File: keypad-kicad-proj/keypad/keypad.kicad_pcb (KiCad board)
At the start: 2 copper layers, 3.5 x 3.1 mm, 115 parts, among them J1 Screw_Terminal_01x02, J2 USB4105-GF-A, J3 USB4105-GF-A, J4 Micro_SD_Card_Det_Hirose_DM3AT, Q1 BC817, Q2 BC817, Q3 IRF9393TRPBF, SW1 RotaryEncoder, SW2 RotaryEncoder, SW25 SW_SPST, SW26 Cherry_MX, SW27 Cherry_MX, SW28 Cherry_MX, SW29 SW_SPST, SW30 SW_SPST, SW31 SW_SPST, SW32 Cherry_MX, SW33 Cherry_MX, SW34 Cherry_MX, SW35 SW_SPST, SW36 SW_SPST, SW37 SW_SPST, SW38 Cherry_MX, SW39 Cherry_MX, SW40 Cherry_MX, SW41 SW_SPST, SW42 SW_SPST, SW43 SW_SPST, SW44 Cherry_MX, SW45 Cherry_MX, SW46 Cherry_MX, SW47 SW_SPST, SW48 SW_SPST, SW49 SW_SPST, U1 ESP32-S3-WROOM-1, U10 SK6812MINI-E, U11 SK6812MINI-E, U12 SK6812MINI-E, U13 SK6812MINI-E, U14 SK6812MINI-E, U2 TLV75901PDRVT, U27 SK6812MINI-E, U3 CP2102N-A01-GQFN24, U4 SK6812MINI-E, U5 SK6812MINI-E, U6 SK6812MINI-E, U7 SK6812MINI-E, U8 SK6812MINI-E, U9 SK6812MINI-E

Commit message: inital pcb layout
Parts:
- SW25: value SW_SPST -> SW_RST; footprint Button_Switch_THT:SW_PUSH-12mm_Wuerth-430476085716 -> Button_Switch_THT:SW_PUSH_6mm
- moved S1 239.4 mm to (263.9, 81.8), turned to 90 degrees
- moved SW26 168.1 mm to (187.3, 74.2)
- moved SW44 168.1 mm to (238.7, 74.2)
- moved SW32 168.1 mm to (204.4, 74.2)
- moved SW33 168.1 mm to (204.4, 91.3)
- moved SW34 168.1 mm to (204.4, 108.5)
- moved SW38 168.1 mm to (221.6, 74.2)
- moved SW39 168.1 mm to (221.6, 91.3)
- moved SW40 168.1 mm to (221.6, 108.5)
- moved SW27 168.1 mm to (187.3, 91.3)
- moved SW28 168.1 mm to (187.3, 108.5)
- moved SW45 168.1 mm to (238.7, 91.3)
- moved SW46 168.1 mm to (238.7, 108.5)
- moved SW1 148.6 mm to (254.5, 48.5), turned to -90 degrees
- moved J3 143.1 mm to (217.2, 30.7), turned to 180 degrees
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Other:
- board size 3.5 x 3.1 mm -> 100 x 100 mm

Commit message: pcb layout update
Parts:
- Brd1: footprint Connector_PinHeader_1.00mm:PinHeader_1x04_P1.00mm_Vertical -> PUT_RocketLab_other:128x64OLED_V2
- C1, C10, C11, C12, C13, C14, C2, C3, C4, C5, C6, C7, C8, C9, D14, D15, D16, D17, D18, D20, D22, D23, D24, D25, D28, D29, D30, D31, D32, D33, D34, D35, D36, D37, D38, D39, J1, J4, Q1, Q2, Q3, R1, R10, R11, R12, R13, R14, R15, R16, R17, R18, R19, R2, R20, R21, R3, R4, R5, R6, R7, R8, R9, U1, U10, U11, U12, U13, U14, U2, U27, U3, U4, U5, U6, U7, U8, U9: moved to B.Cu
- moved J3 242.0 mm to (-24.4, 42.9)
- moved J2 204.9 mm to (-17.7, 161.2), turned to 180 degrees
- moved D18 172.2 mm to (-21.7, 54.0), turned to 90 degrees
- moved R5 166.1 mm to (-23.3, 59.0), turned to -90 degrees
- moved R7 162.8 mm to (-23.0, 62.1), turned to -90 degrees
- moved C5 159.8 mm to (-20.8, 62.1), turned to -90 degrees
- moved Q3 157.9 mm to (156.4, 50.0)
- moved U2 156.1 mm to (166.1, 57.5)
- moved D16 154.4 mm to (-20.8, 171.0), turned to -90 degrees
- moved R10 153.4 mm to (-1.00, 45.6), turned to 90 degrees
- moved D15 153.1 mm to (-18.5, 171.0), turned to -90 degrees
- moved SW30 151.8 mm to (-45.0, 225.5)
- moved SW36 151.8 mm to (-28.0, 225.5)
- moved SW42 151.8 mm to (-10.9, 225.5)
- moved SW48 151.8 mm to (6.15, 225.5)
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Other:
- board size 100 x 100 mm -> 169.5 x 132.2 mm

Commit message: full inital pcb layout
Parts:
- D19, D21: moved to B.Cu
- moved J2 190.2 mm to (130.9, 42.5)
- moved D15 190.2 mm to (130.1, 52.3)
- moved D16 190.2 mm to (127.7, 52.3)
- moved D17 190.2 mm to (133.9, 53.9)
- moved Q1 111.9 mm to (98.9, 88.7)
- moved R10 111.9 mm to (102.1, 89.1)
- moved R7 109.9 mm to (83.4, 89.6), turned to 0 degrees
- moved R5 108.1 mm to (80.3, 89.9), turned to 0 degrees
- moved C5 107.3 mm to (83.4, 87.4), turned to 0 degrees
- moved D18 102.8 mm to (75.3, 88.2), turned to 180 degrees
- moved D21 100.9 mm to (83.2, 81.2)
- moved D19 99.8 mm to (83.2, 78.6)
- moved J3 97.9 mm to (63.9, 85.2), turned to -90 degrees
- moved Q2 97.5 mm to (91.6, 88.4)
- moved R11 97.5 mm to (95.0, 88.9)
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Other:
- board size 169.5 x 132.2 mm -> 132.9 x 112.7 mm

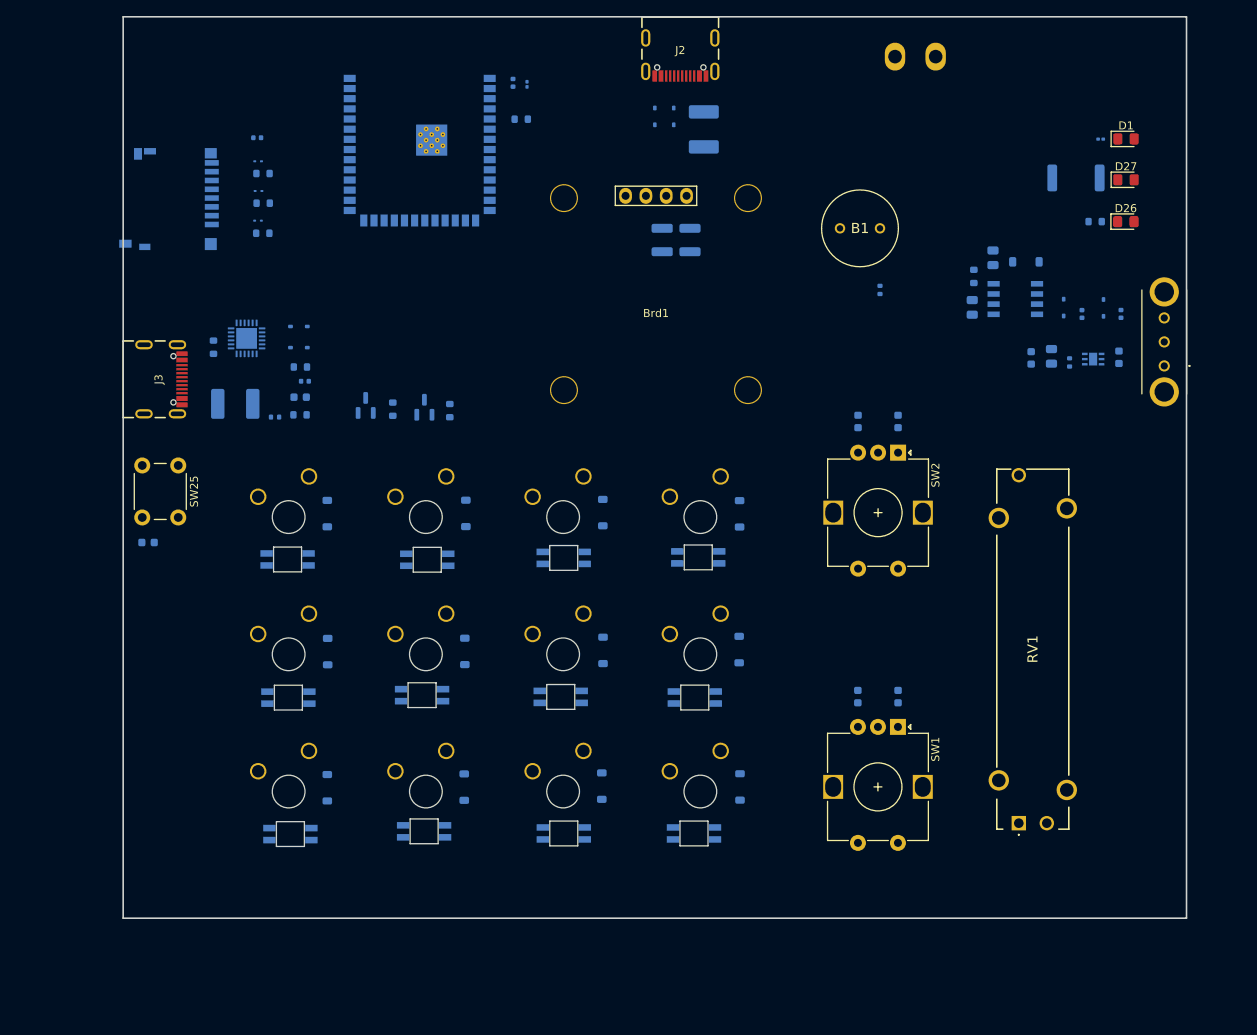
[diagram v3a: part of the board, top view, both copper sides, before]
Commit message: update keys alignment
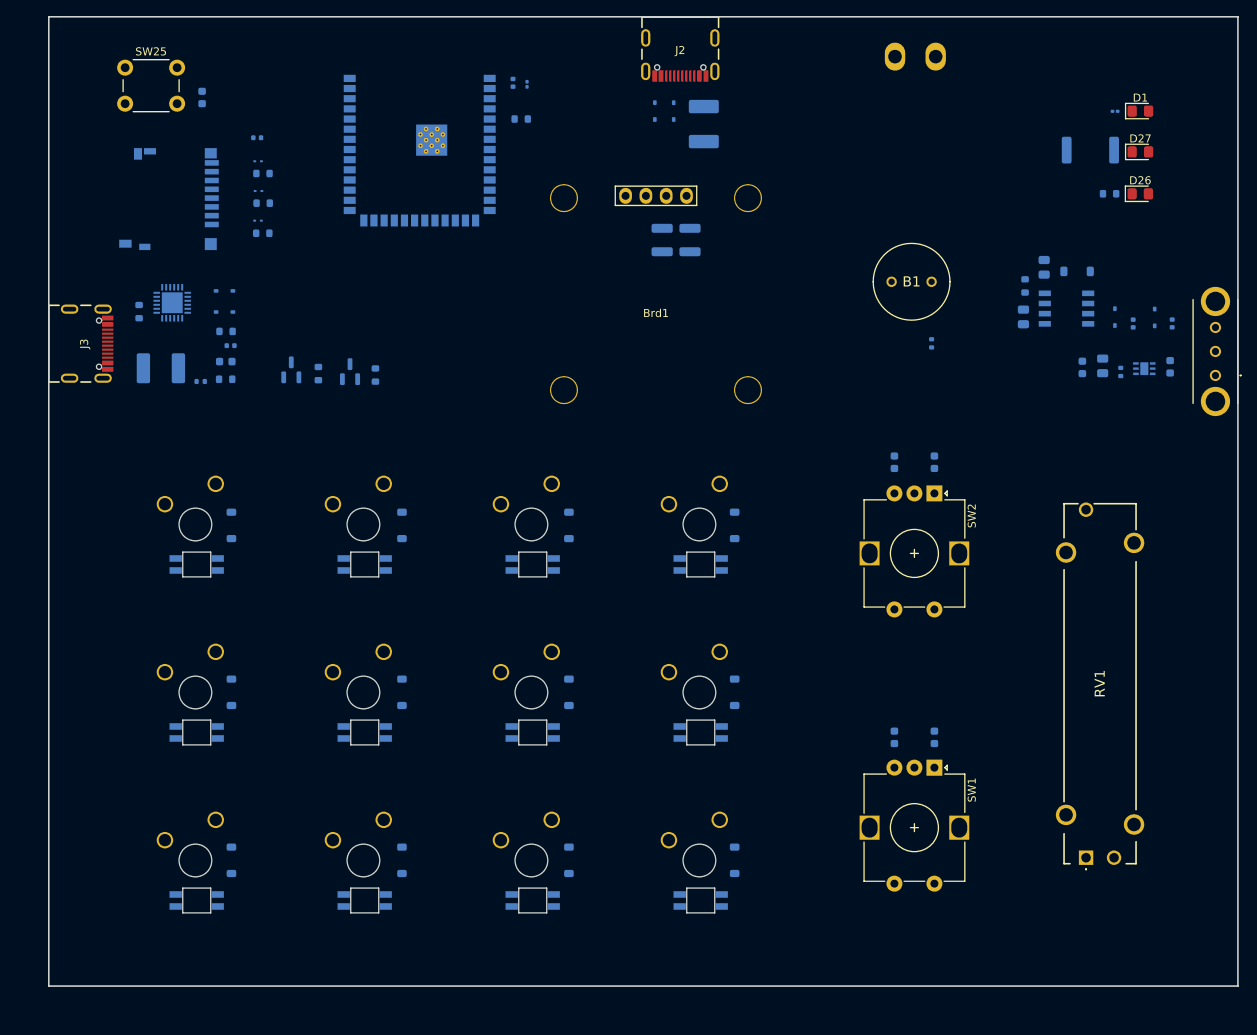
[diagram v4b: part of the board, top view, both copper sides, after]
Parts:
- moved C9 56.0 mm to (71.1, 49.9), turned to 90 degrees
- moved SW25 50.2 mm to (61.5, 46.2), turned to 0 degrees
- moved D30 15.0 mm to (74.8, 145.3)
- moved SW28 14.5 mm to (66.5, 142.8)
- moved U12 14.4 mm to (70.5, 150.3)
- moved D29 13.1 mm to (74.8, 124.3)
- moved SW27 12.6 mm to (66.5, 121.8)
- moved U8 12.3 mm to (70.5, 129.3)
- moved D28 12.1 mm to (74.8, 103.4)
- moved D33 12.0 mm to (96.1, 145.3)
- moved SW26 11.7 mm to (66.5, 100.8)
- moved SW34 11.6 mm to (87.5, 142.8)
- moved U13 11.4 mm to (91.5, 150.3)
- moved U4 11.4 mm to (70.5, 108.3)
- moved C5 10.3 mm to (74.1, 82.9)
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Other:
- board size 132.9 x 112.7 mm -> 148.6 x 121.2 mm

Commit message: main layout
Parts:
- C10, C3, C4, C6, C7: footprint Capacitor_SMD:C_0402_1005Metric -> Capacitor_SMD:C_0603_1608Metric
- C8: footprint Capacitor_SMD:C_0201_0603Metric -> Capacitor_SMD:C_0603_1608Metric
- R16: footprint Resistor_SMD:R_0201_0603Metric -> Resistor_SMD:R_0603_1608Metric
- R18: footprint Resistor_SMD:R_2512_6332Metric -> Resistor_SMD:R_0805_2012Metric
- R19, R5: footprint Resistor_SMD:R_0402_1005Metric -> Resistor_SMD:R_0603_1608Metric
- R3: footprint Resistor_SMD:R_0402_1005Metric -> Resistor_SMD:R_0805_2012Metric
- moved SW29 112.8 mm to (67.8, 213.5)
- moved SW30 112.8 mm to (67.8, 227.1)
- moved SW31 112.8 mm to (67.8, 240.6)
- moved SW35 112.8 mm to (84.8, 213.5)
- moved SW36 112.8 mm to (84.8, 227.1)
- moved SW37 112.8 mm to (84.8, 240.6)
- moved SW41 112.8 mm to (101.9, 213.5)
- moved SW42 112.8 mm to (101.9, 227.1)
- moved SW43 112.8 mm to (101.9, 240.6)
- moved SW47 112.8 mm to (118.9, 213.5)
- moved SW48 112.8 mm to (118.9, 227.1)
- moved SW49 112.8 mm to (118.9, 240.6)
- moved SW25 57.6 mm to (53.3, 103.3), turned to 90 degrees
- moved C9 45.7 mm to (57.1, 93.4), turned to 180 degrees
- moved Q2 13.7 mm to (79.4, 70.6)
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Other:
- board size 148.6 x 121.2 mm -> 160 x 125 mm

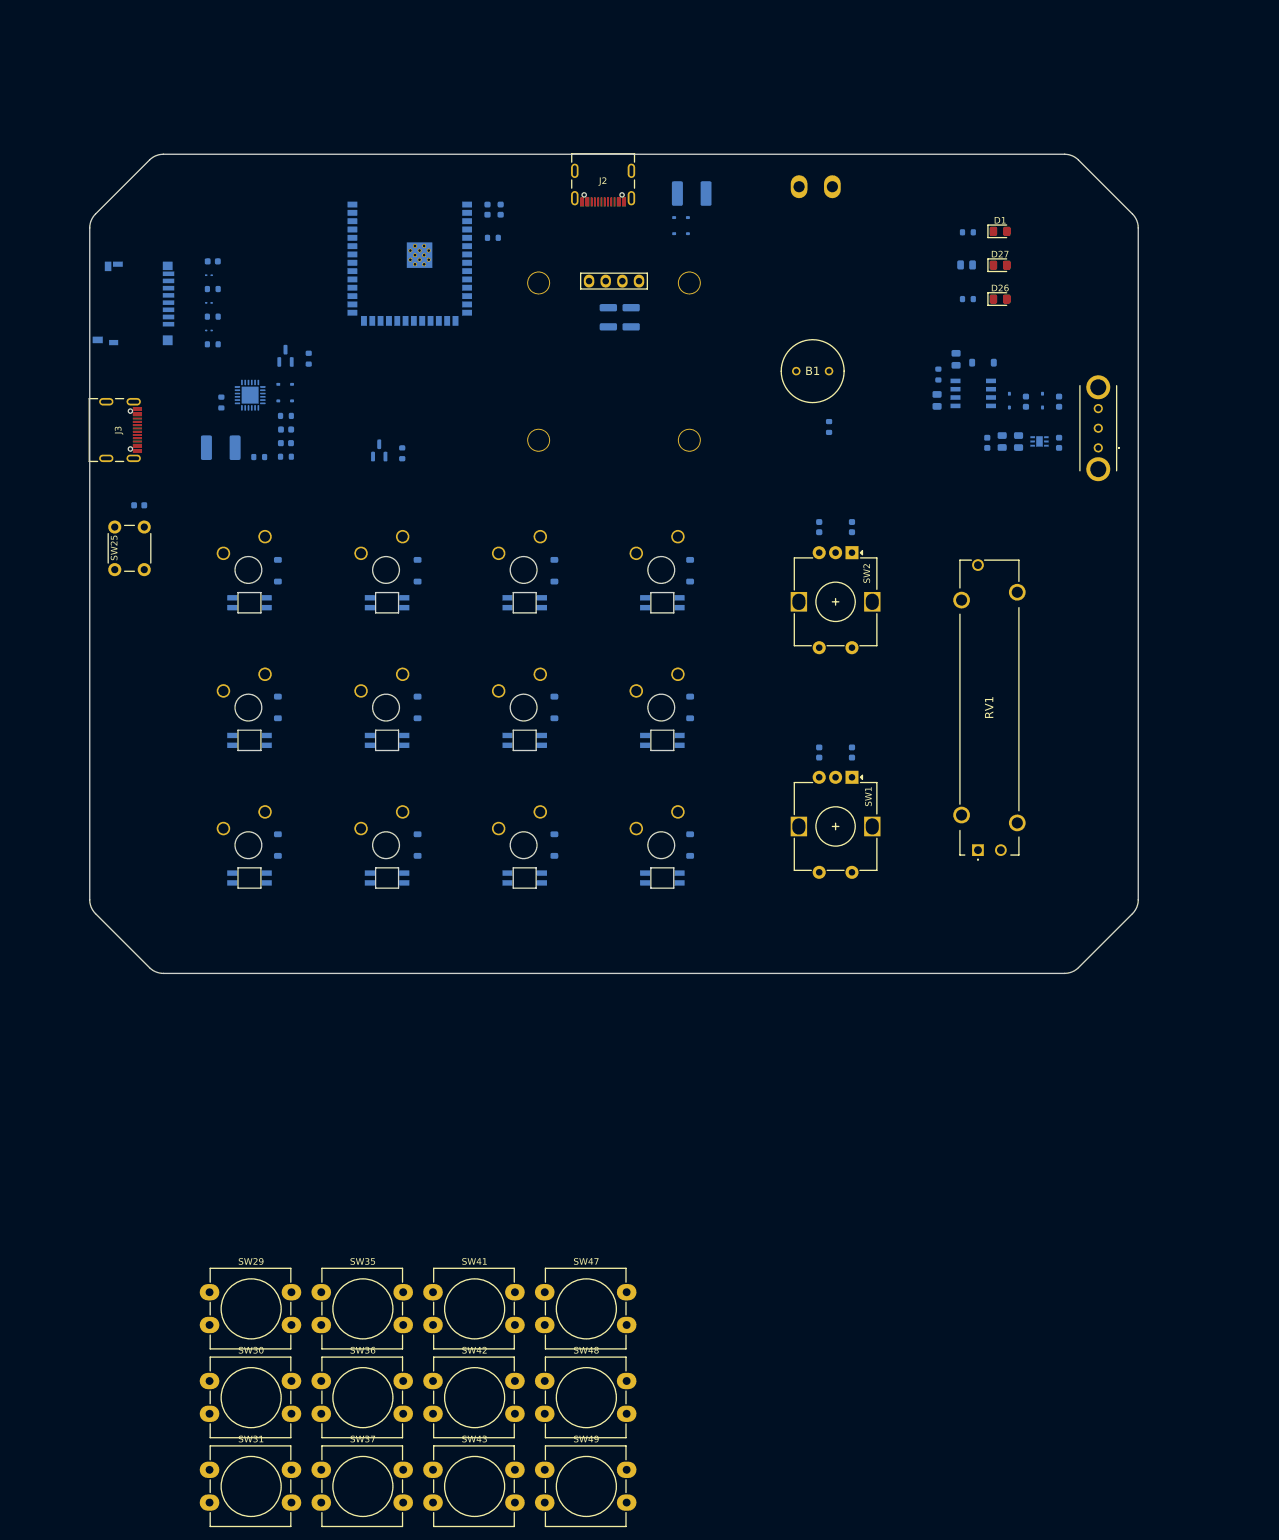
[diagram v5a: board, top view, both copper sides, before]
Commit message: rm keypad 2ndary btns
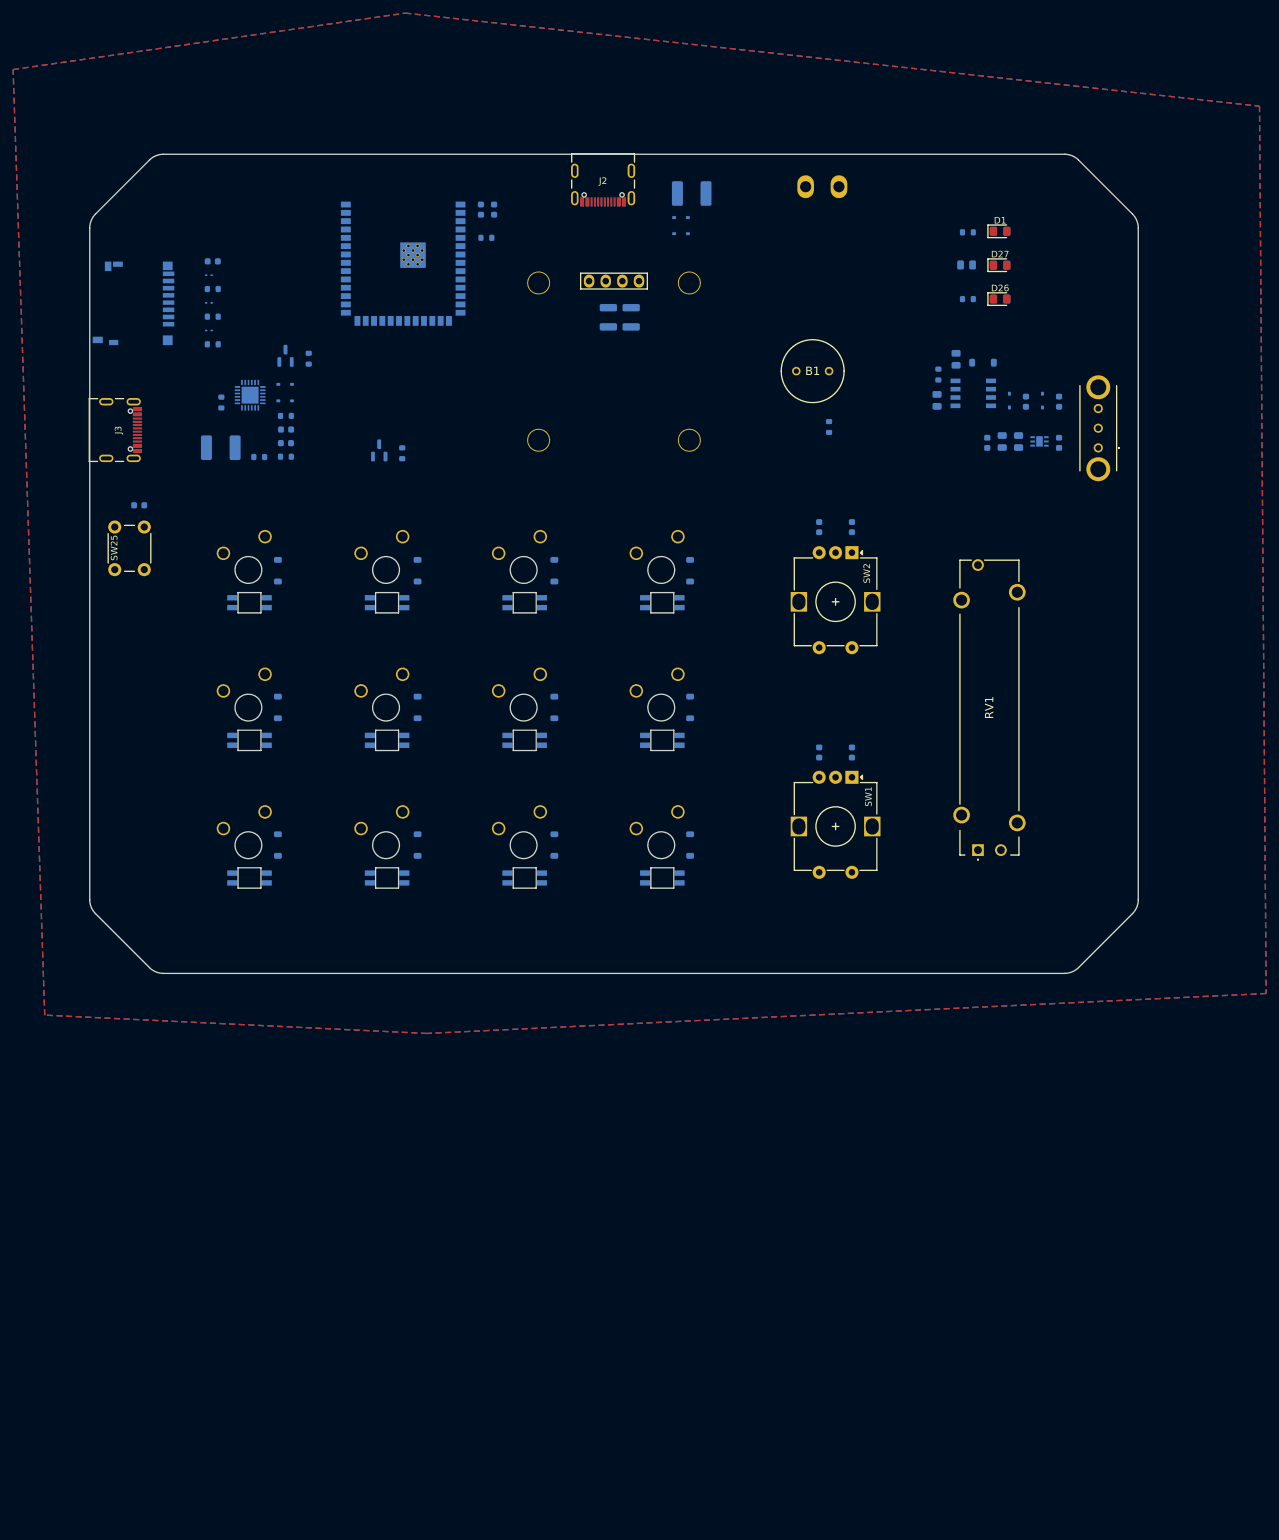
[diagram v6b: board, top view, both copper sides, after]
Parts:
- removed SW29, SW30, SW31, SW35, SW36, SW37, SW41, SW42, SW43, SW47, SW48, SW49: SW_SPST, Button_Switch_THT:SW_PUSH-12mm_Wuerth-430476085716
- moved C7 1.00 mm to (109.2, 48.3)
- moved C8 1.00 mm to (111.2, 48.3)
- moved J1 1.00 mm to (161.3, 44.8)
- moved R20 1.00 mm to (110.0, 52.6)
- moved U1 1.00 mm to (97.3, 52.8)
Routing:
- added copper zone on B.Cu, net GND
- added copper zone on F.Cu, net GND
